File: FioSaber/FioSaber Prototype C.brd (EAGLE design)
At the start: 26.7 x 53.6 mm, 20 parts, among them P1 WIICHUCK, T1 2N2222

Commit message: fixed switch issue
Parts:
- turned SWITCH to 90 degrees
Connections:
- net N$1: no longer SWITCH.1
- net N$7: now also SWITCH.1; no longer SWITCH.2
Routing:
- net N$12: track 24.9 -> 13.6 mm, vias 3 -> 0
- net N$6: track 38.5 -> 32.3 mm, vias 3 -> 1
- net N$25: track 35.8 -> 39.2 mm, vias 2 -> 4
- net N$7: track 76.4 -> 73.7 mm
- net N$8: track 38.4 -> 41.1 mm, vias 3 -> 5
- net N$4: track 39.8 -> 41.7 mm, vias 3 -> 2
- net N$18: track 40.9 -> 40.1 mm, vias 6 -> 2
- net N$1: track 63.6 -> 62.9 mm, vias 5 -> 6
- net N$3: track 43.9 -> 44.3 mm, vias 1 -> 2
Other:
- board text added: "Prototype C2"
- board text removed: "Prototype C"

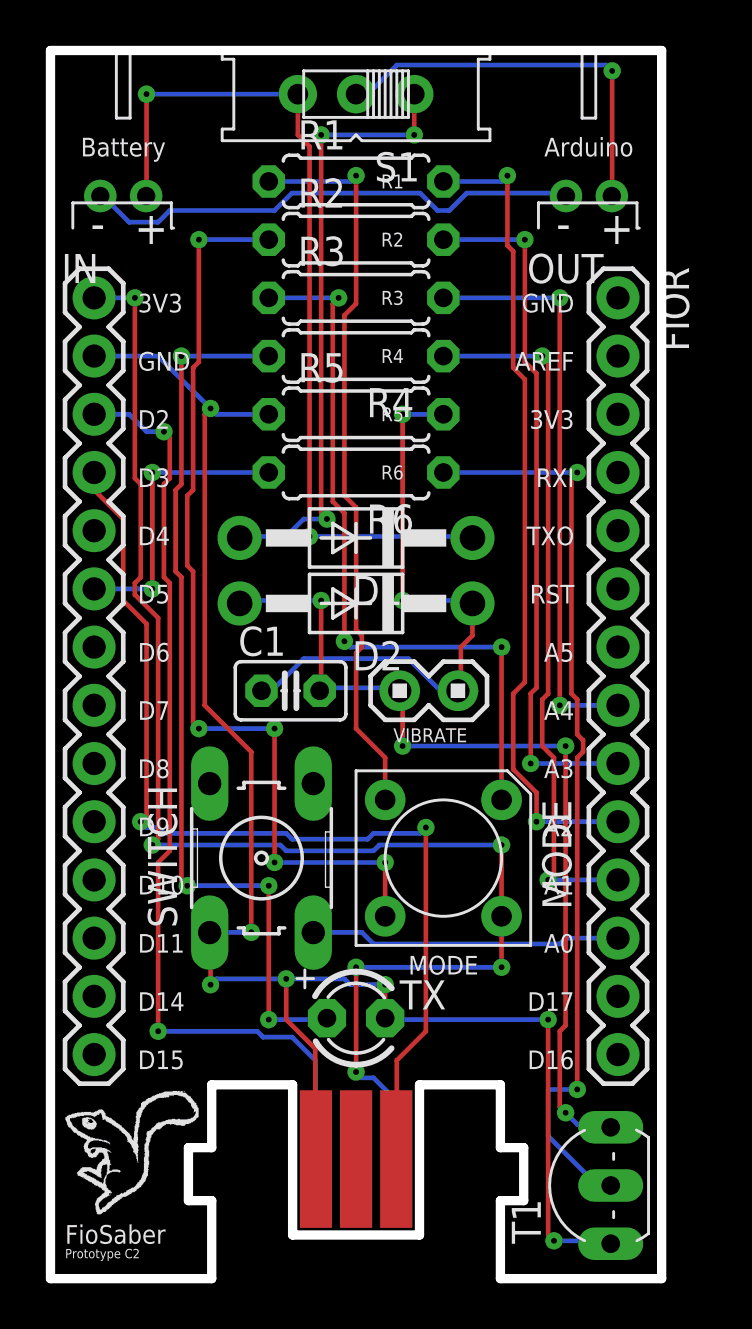
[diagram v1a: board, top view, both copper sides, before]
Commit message: fixed haptic circuit, prototype c3 for fab
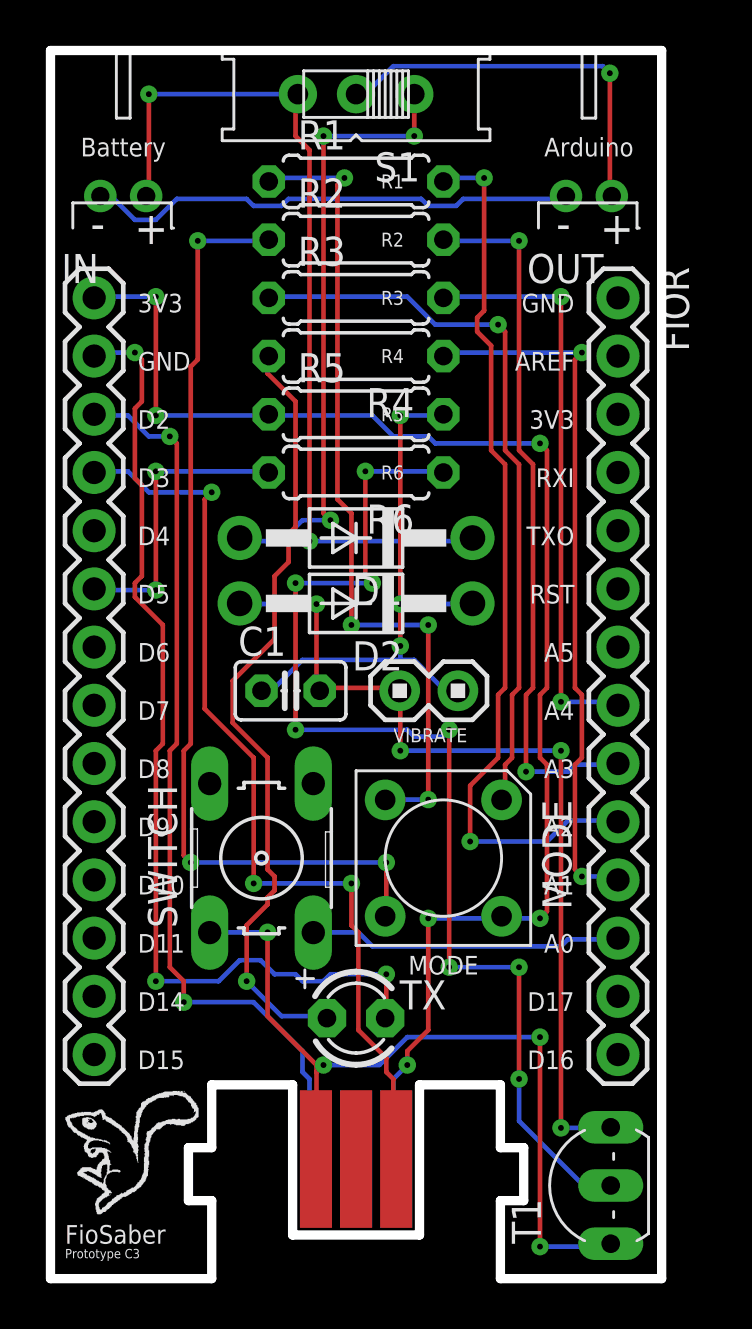
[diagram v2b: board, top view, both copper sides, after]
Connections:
- new net N$24: FIOL.2, TX.K
- net N$1: now also R5.1
- net N$7: no longer FIOL.2, R5.1, TX.K
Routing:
- net N$24: track 0.00 -> 43.3 mm, vias 0 -> 3
- net N$7: track 73.7 -> 36.0 mm, vias 7 -> 4
- net N$18: track 40.1 -> 50.4 mm, vias 2 -> 8
- net N$25: track 39.2 -> 34.4 mm, vias 4 -> 1
- net N$6: track 32.3 -> 36.1 mm, vias 1 -> 4
- net N$3: track 44.3 -> 40.7 mm, vias 2 -> 3
- net N$13: track 35.6 -> 38.9 mm
- net N$4: track 41.7 -> 39.9 mm
- net N$20: track 26.9 -> 25.4 mm, vias 2 -> 3
- net N$8: track 41.1 -> 41.5 mm, vias 5 -> 3
- net N$9: vias 3 -> 1
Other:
- board text added: "Prototype C3"
- board text removed: "Prototype C2"

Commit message: FioSaber Prototype C4
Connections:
- removed net N$7: P1.SCL, SWITCH.1, T1.E
- net N$24: now also P1.SCL, SWITCH.1
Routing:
- net N$7: track 36.0 -> 0.00 mm, vias 4 -> 0
- net N$24: track 43.3 -> 54.3 mm, vias 3 -> 4
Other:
- board text added: "Prototype C4"
- board text removed: "Prototype C3"
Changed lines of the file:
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@@
 <text x="22.86" y="51.435" size="0.8128" layer="21" font="vector" ratio="15" rot="SR0" align="top-center">Arduino</text>
 <text x="0" y="3.175" size="0.8128" layer="21" font="vector" ratio="15" rot="SR0">FioSaber</text>
-<text x="0" y="2.54" size="0.4064" layer="21" font="vector" ratio="15" rot="SR0">Prototype C3</text>
+<text x="0" y="2.54" size="0.4064" layer="21" font="vector" ratio="15" rot="SR0">Prototype C4</text>
 <rectangle x1="1.4097" y1="4.4577" x2="1.5621" y2="4.4831" layer="21"/>
 <rectangle x1="1.3843" y1="4.4831" x2="1.6129" y2="4.5085" layer="21"/>
@@
 <via x="7.9248" y="14.6304" extent="1-16" drill="0.254"/>
 </signal>
-<signal name="N$7">
-<contactref element="SWITCH" pad="1"/>
-<contactref element="T1" pad="E"/>
-<contactref element="P1" pad="SCL"/>
-<wire x1="20.7264" y1="3.048" x2="23.7744" y2="3.048" width="0.2032" layer="16"/>
-<wire x1="20.7264" y1="12.192" x2="20.7264" y2="3.048" width="0.2032" layer="1"/>
-<wire x1="14.9352" y1="12.192" x2="20.7264" y2="12.192" width="0.2032" layer="16"/>
-<wire x1="13.716" y1="10.9728" x2="14.9352" y2="12.192" width="0.2032" layer="16"/>
-<wire x1="11.2776" y1="10.9728" x2="13.716" y2="10.9728" width="0.2032" layer="16"/>
-<wire x1="10.9728" y1="10.668" x2="11.2776" y2="10.9728" width="0.2032" layer="1"/>
-<wire x1="10.9728" y1="7.0104" x2="10.9728" y2="10.668" width="0.2032" layer="1"/>
-<wire x1="23.7744" y1="3.048" x2="23.8125" y2="3.175" width="0.2032" layer="16"/>
-<wire x1="10.9728" y1="7.0104" x2="10.95" y2="6.87" width="0.2032" layer="1"/>
-<wire x1="8.8392" y1="16.764" x2="6.4008" y2="16.764" width="0.2032" layer="16"/>
-<wire x1="8.8392" y1="13.1064" x2="8.8392" y2="16.764" width="0.2032" layer="1"/>
-<wire x1="10.9728" y1="10.9728" x2="8.8392" y2="13.1064" width="0.2032" layer="1"/>
-<wire x1="10.9728" y1="10.668" x2="10.9728" y2="10.9728" width="0.2032" layer="1"/>
-<wire x1="6.4008" y1="16.764" x2="6.3119" y2="16.7513" width="0.2032" layer="16"/>
-<via x="20.7264" y="3.048" extent="1-16" drill="0.254"/>
-<via x="20.7264" y="12.192" extent="1-16" drill="0.254"/>
-<via x="11.2776" y="10.9728" extent="1-16" drill="0.254"/>
-<via x="8.8392" y="16.764" extent="1-16" drill="0.254"/>
-</signal>
 <signal name="N$6">
 <contactref element="MODE" pad="2"/>
@@
 <wire x1="8.5344" y1="15.5448" x2="7.62" y2="15.5448" width="0.2032" layer="16"/>
 <wire x1="9.144" y1="14.9352" x2="8.5344" y2="15.5448" width="0.2032" layer="16"/>
-<wire x1="10.0584" y1="14.9352" x2="9.144" y2="14.9352" width="0.2032" layer="16"/>
+<wire x1="10.0584" y1="14.9352" x2="9.4488" y2="14.9352" width="0.2032" layer="16"/>
+<wire x1="9.4488" y1="14.9352" x2="9.144" y2="14.9352" width="0.2032" layer="16"/>
 <wire x1="10.3632" y1="14.6304" x2="10.0584" y2="14.9352" width="0.2032" layer="16"/>
 <wire x1="11.2776" y1="14.6304" x2="10.3632" y2="14.6304" width="0.2032" layer="16"/>
@@
 <via x="3.9624" y="14.6304" extent="1-16" drill="0.254"/>
 <via x="14.0208" y="14.9352" extent="1-16" drill="0.254"/>
+<contactref element="P1" pad="SCL"/>
+<contactref element="SWITCH" pad="1"/>
+<wire x1="7.3152" y1="15.5448" x2="6.4008" y2="16.4592" width="0.2032" layer="16"/>
+<wire x1="7.62" y1="15.5448" x2="7.3152" y2="15.5448" width="0.2032" layer="16"/>
+<wire x1="6.4008" y1="16.4592" x2="6.3119" y2="16.7513" width="0.2032" layer="16"/>
+<wire x1="9.4488" y1="11.2776" x2="9.4488" y2="14.9352" width="0.2032" layer="1"/>
+<wire x1="10.0584" y1="10.668" x2="9.4488" y2="11.2776" width="0.2032" layer="1"/>
+<wire x1="10.668" y1="10.668" x2="10.0584" y2="10.668" width="0.2032" layer="1"/>
+<wire x1="10.668" y1="7.0104" x2="10.668" y2="10.668" width="0.2032" layer="1"/>
+<wire x1="10.668" y1="7.0104" x2="10.95" y2="6.87" width="0.2032" layer="1"/>
+<via x="9.4488" y="14.9352" extent="1-16" drill="0.254"/>
 </signal>
 </signals>
